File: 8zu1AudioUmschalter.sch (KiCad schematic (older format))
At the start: 59 parts, among them IC1 ATMEGA8A-A, IC2 MAX9890, J1 USB, J2 LUM 1503-07, J3 LUM 1503-07, J4 LUM 1503-07, J5 LUM 1503-07, J6 LUM 1503-07, J7 LUM 1503-07, J8 LUM 1503-07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

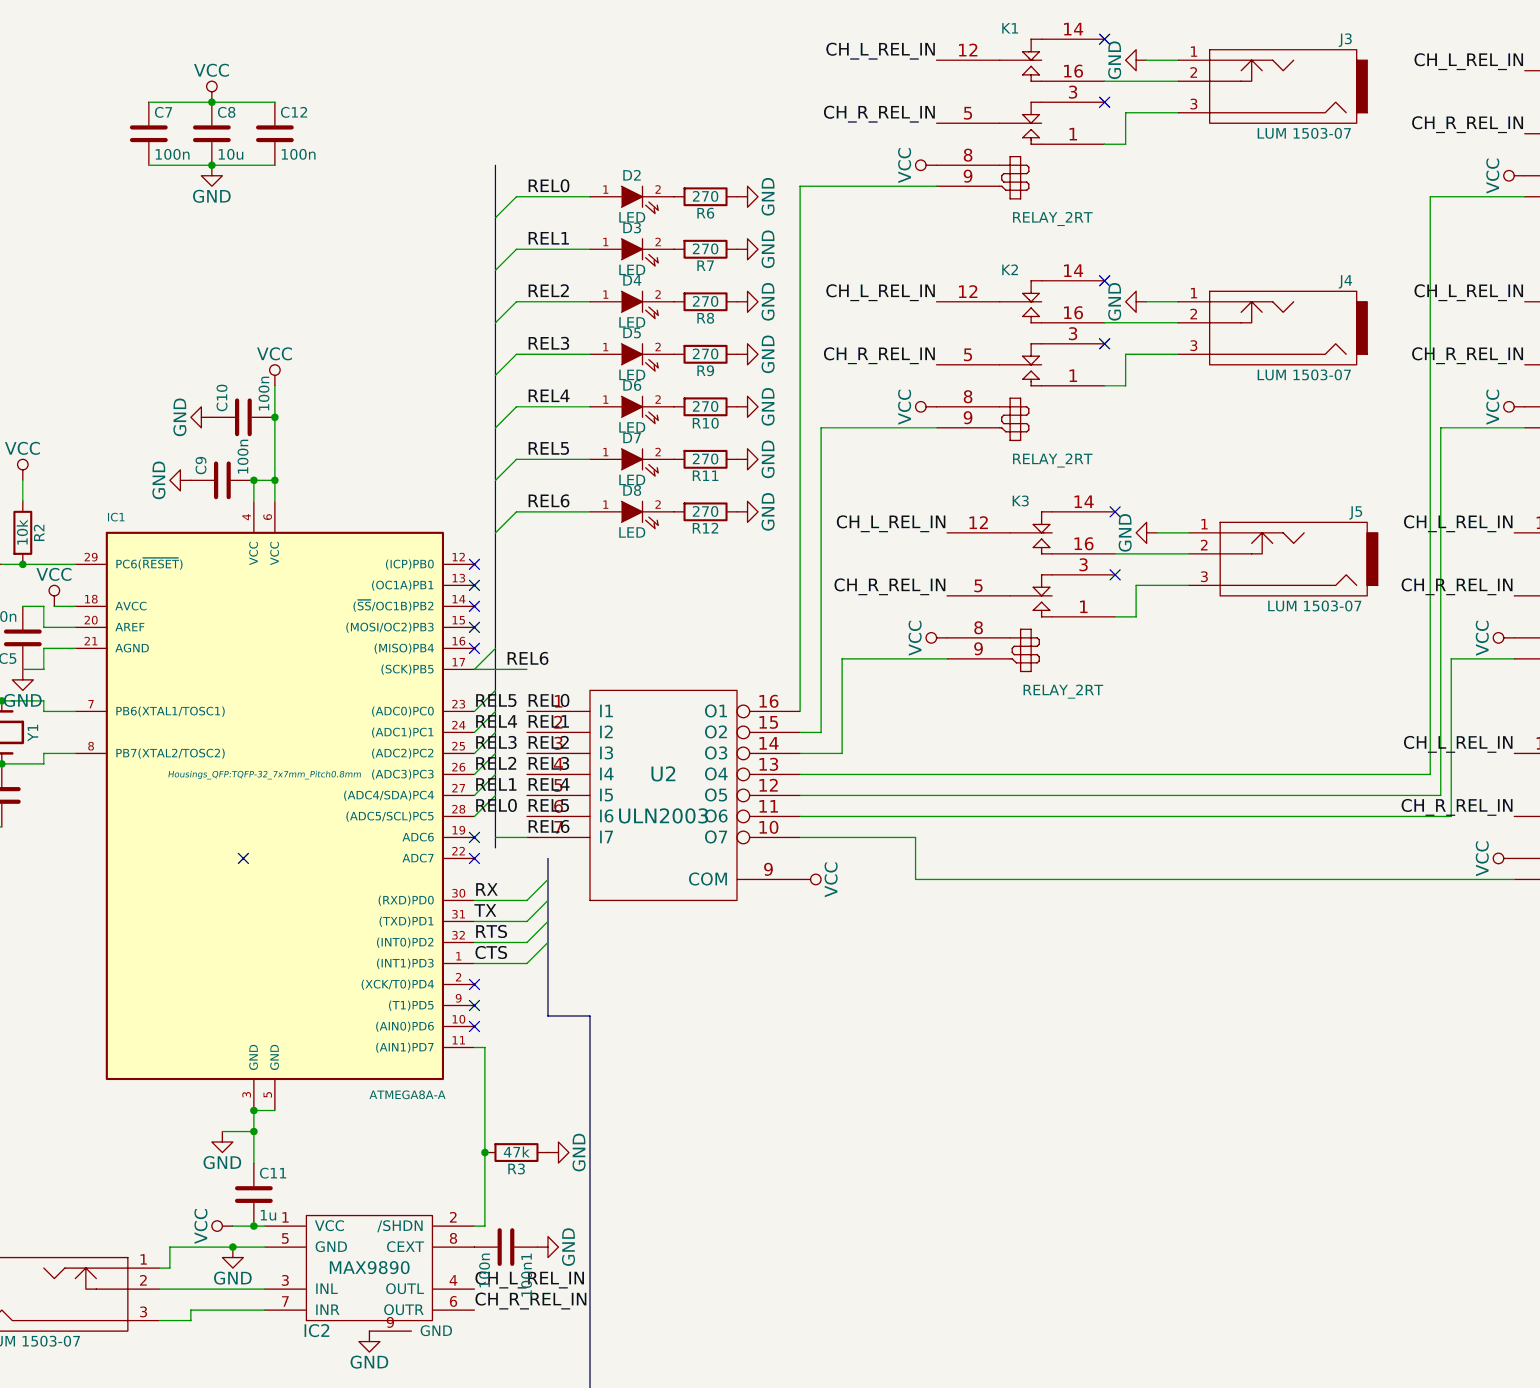
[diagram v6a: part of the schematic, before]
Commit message: Kleinere Änderungen und Hinzufügen des TMP75
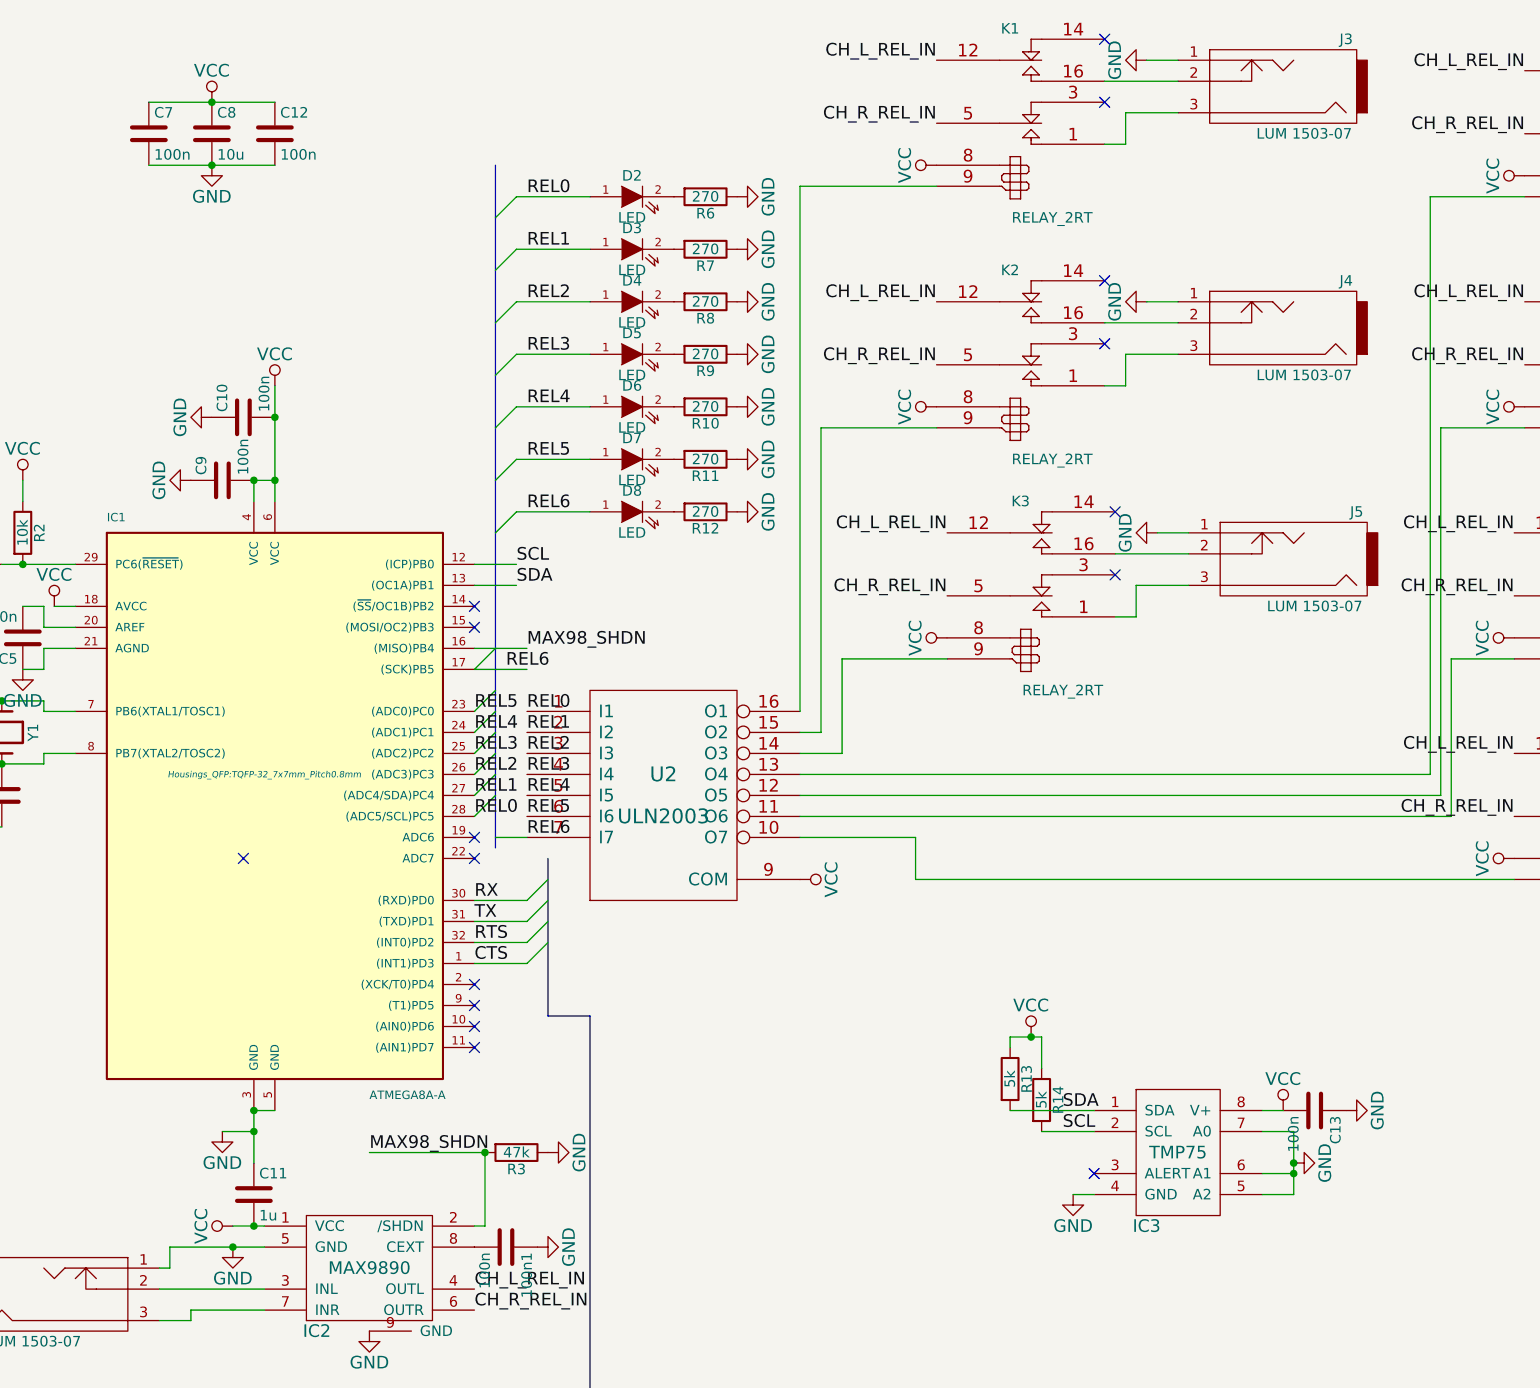
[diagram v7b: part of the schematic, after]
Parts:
- added C13: 100n, Capacitors_SMD:C_0603, symbol C
- added IC3: TMP75, SMD_Packages:SOIC-8-N, symbol TMP75
- added R13, R14: 5k, Resistors_SMD:R_0603, symbol R
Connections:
- net GND: now also C13.1, IC3.4 (GND), IC3.5 (A2), IC3.6 (A1), IC3.7 (A0)
- net VCC: now also C13.2, IC3.8 (V+), R13.1, R14.1
- net MAX98_SHDN: now reaches IC2.2 (/SHDN), R3.2
- net MAX98_SHDN: now also IC1.16 ((MISO)PB4); no longer IC1.11 ((AIN1)PD7)
- net SCL: now reaches IC1.12 ((ICP)PB0)
- net SCL: now also IC3.2 (SCL), R14.2
- net SDA: now reaches IC1.13 ((OC1A)PB1)
- net SDA: now also IC3.1 (SDA), R13.2
- no-connect marks 36 -> 35
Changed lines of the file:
@@
 LIBS:max9890
 LIBS:ft232rl
+LIBS:tmp75
 LIBS:8zu1AudioUmschalter-cache
 EELAYER 25 0
@@
 	8300 6750 8250 6750
 Wire Wire Line
-	8300 5900 8300 6750
-Wire Wire Line
-	8300 5900 8250 5900
+	8300 6400 8300 6750
 Wire Wire Line
 	6350 9850 6150 9850
@@
 	6700 1700 7300 1700
 Wire Wire Line
-	7300 1400 6700 1400
+	6700 1400 7300 1400
 $Comp
 L GND #PWR07
@@
 Connection ~ 6000 4550
 Connection ~ 6000 4250
-NoConn ~ 8250 5700
-NoConn ~ 8250 4000
 NoConn ~ 8250 3900
 $Comp
@@
 	0    -1   -1   0
 $EndComp
-NoConn ~ 8250 5600
 $Comp
 L C 100n1
@@
 	6300 7750 6300 8200
 NoConn ~ 8250 3800
-NoConn ~ 8250 3700
-NoConn ~ 8250 3600
 Entry Wire Line
 	8250 4800 8350 4700
@@
 $EndComp
 NoConn ~ 13700 8750
+$Comp
+L TMP75 IC3
+U 1 1 550C7FC6
+P 11600 6400
+F 0 "IC3" H 11450 6050 60  0000 C CNN
+F 1 "TMP75" H 11600 6400 60  0000 C CNN
+F 2 "SMD_Packages:SOIC-8-N" H 11600 6400 60  0001 C CNN
+F 3 "" H 11600 6400 60  0000 C CNN
+	1    11600 6400
+	1    0    0    -1
+$EndComp
+$Comp
+L GND #PWR047
+U 1 1 550C84D9
+P 12150 6450
+F 0 "#PWR047" H 12150 6200 60  0001 C CNN
+F 1 "GND" H 12150 6300 60  0000 C CNN
+F 2 "" H 12150 6450 60  0000 C CNN
+F 3 "" H 12150 6450 60  0000 C CNN
+	1    12150 6450
+	0    -1   -1   0
+$EndComp
+Wire Wire Line
+	12150 6600 12000 6600
+Wire Wire Line
+	12150 6300 12150 6600
+Wire Wire Line
+	12000 6300 12150 6300
+Connection ~ 12150 6450
+Wire Wire Line
+	12000 6500 12150 6500
+Connection ~ 12150 6500
+NoConn ~ 11200 6500
+$Comp
+L VCC #PWR048
+U 1 1 550C899A
+P 12100 6200
+F 0 "#PWR048" H 12100 6050 60  0001 C CNN
+F 1 "VCC" H 12100 6350 60  0000 C CNN
+F 2 "" H 12100 6200 60  0000 C CNN
+F 3 "" H 12100 6200 60  0000 C CNN
+	1    12100 6200
+	1    0    0    -1
+$EndComp
+Wire Wire Line
+	12100 6200 12000 6200
+NoConn ~ 8250 5700
+NoConn ~ 8250 5600
+NoConn ~ 8250 5900
+Text Label 7750 6400 0    60   ~ 0
+MAX98_SHDN
+Wire Wire Line
+	8300 6400 7750 6400
+Text Label 8500 4000 0    60   ~ 0
+MAX98_SHDN
+Wire Wire Line
+	8250 4000 8500 4000
+Wire Wire Line
+	8250 3600 8450 3600
+Wire Wire Line
+	8250 3700 8450 3700
+Text Label 8450 3600 0    60   ~ 0
+SCL
+Text Label 8450 3700 0    60   ~ 0
+SDA
+$Comp
+L GND #PWR049
+U 1 1 550CADEA
+P 11100 6600
+F 0 "#PWR049" H 11100 6350 60  0001 C CNN
+F 1 "GND" H 11100 6450 60  0000 C CNN
+F 2 "" H 11100 6600 60  0000 C CNN
+F 3 "" H 11100 6600 60  0000 C CNN
+	1    11100 6600
+	1    0    0    -1
+$EndComp
+Wire Wire Line
+	11200 6600 11100 6600
+Wire Wire Line
+	10800 6200 11200 6200
+Text Label 11050 6300 0    60   ~ 0
+SCL
+Text Label 11050 6200 0    60   ~ 0
+SDA
+$Comp
+L R R14
+U 1 1 550CC98F
+P 10950 6150
+F 0 "R14" V 11030 6150 50  0000 C CNN
+F 1 "5k" V 10950 6150 50  0000 C CNN
+F 2 "Resistors_SMD:R_0603" V 10880 6150 30  0001 C CNN
+F 3 "" H 10950 6150 30  0000 C CNN
+	1    10950 6150
+	1    0    0    -1
+$EndComp
+$Comp
+L R R13
+U 1 1 550CCAFA
+P 10800 6050
+F 0 "R13" V 10880 6050 50  0000 C CNN
+F 1 "5k" V 10800 6050 50  0000 C CNN
+F 2 "Resistors_SMD:R_0603" V 10730 6050 30  0001 C CNN
+F 3 "" H 10800 6050 30  0000 C CNN
+	1    10800 6050
+	1    0    0    -1
+$EndComp
+$Comp
+L VCC #PWR050
+U 1 1 550CCCB3
+P 10900 5850
+F 0 "#PWR050" H 10900 5700 60  0001 C CNN
+F 1 "VCC" H 10900 6000 60  0000 C CNN
+F 2 "" H 10900 5850 60  0000 C CNN
+F 3 "" H 10900 5850 60  0000 C CNN
+	1    10900 5850
+	1    0    0    -1
+$EndComp
+Wire Wire Line
+	10950 6000 10950 5850
+Wire Wire Line
+	10950 5850 10800 5850
+Wire Wire Line
+	10800 5850 10800 5900
+Connection ~ 10900 5850
+Wire Wire Line
+	11200 6300 10950 6300
+$Comp
+L C C13
+U 1 1 550CFBE5
+P 12250 6200
+F 0 "C13" H 12275 6300 50  0000 L CNN
+F 1 "100n" H 12275 6100 50  0000 L CNN
+F 2 "Capacitors_SMD:C_0603" H 12288 6050 30  0001 C CNN
+F 3 "" H 12250 6200 60  0000 C CNN
+	1    12250 6200
+	0    1    1    0
+$EndComp
+$Comp
+L GND #PWR051
+U 1 1 550D0081
+P 12400 6200
+F 0 "#PWR051" H 12400 5950 60  0001 C CNN
+F 1 "GND" H 12400 6050 60  0000 C CNN
+F 2 "" H 12400 6200 60  0000 C CNN
+F 3 "" H 12400 6200 60  0000 C CNN
+	1    12400 6200
+	0    -1   -1   0
+$EndComp
 $EndSCHEMATC

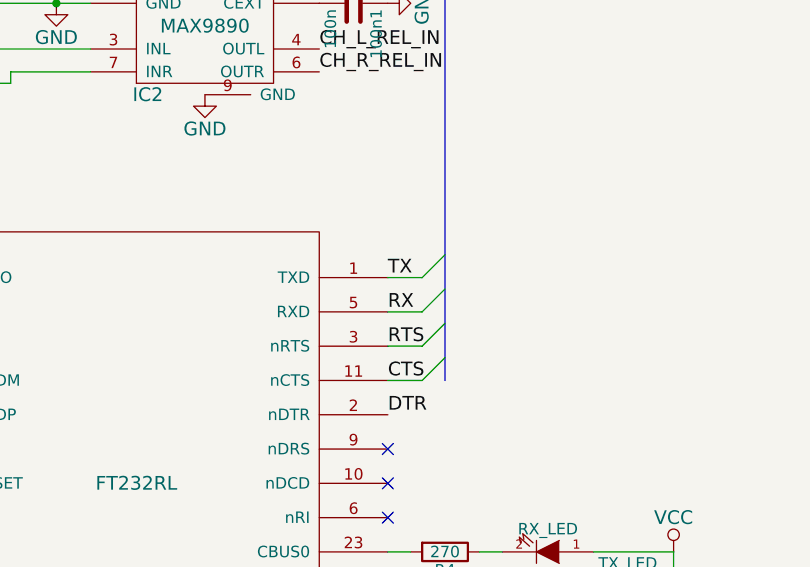
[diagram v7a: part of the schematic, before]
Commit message: Layoutfehler, TX und RX waren nicht gekreuzt.
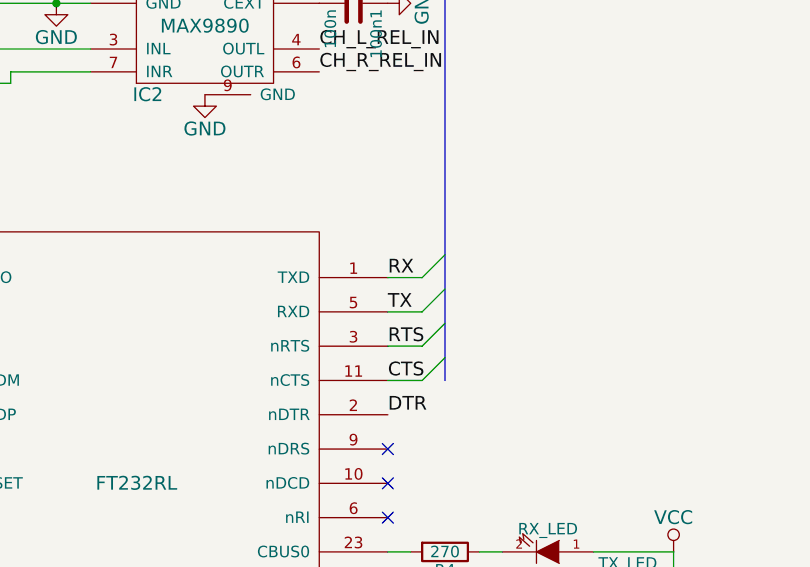
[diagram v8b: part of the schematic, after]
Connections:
- net RX: now also U1.1 (TXD); no longer U1.5 (RXD)
- net TX: now also U1.5 (RXD); no longer U1.1 (TXD)
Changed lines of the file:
@@
 Wire Bus Line
 	8600 5750 8800 5750
+Text Label 8550 8200 0    60   ~ 0
+TX
 Text Label 8550 8050 0    60   ~ 0
-TX
-Text Label 8550 8200 0    60   ~ 0
 RX
 Text Label 8550 8350 0    60   ~ 0
